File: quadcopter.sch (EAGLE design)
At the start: 75 parts, among them J1 AVR_SPI_PRG_6NS, J3 HEADER-0.1IN-2POS-FEMALE, J4 HEADER-0.1IN-2POS-FEMALE, J5 HEADER-0.1IN-2POS-FEMALE, J6 HEADER-0.1IN-2POS-FEMALE, SW1 PUSHBUTTON_SMD-VERTICAL, SW2 PUSHBUTTON_SMD-VERTICAL, U1 ATMEGA128RFA1

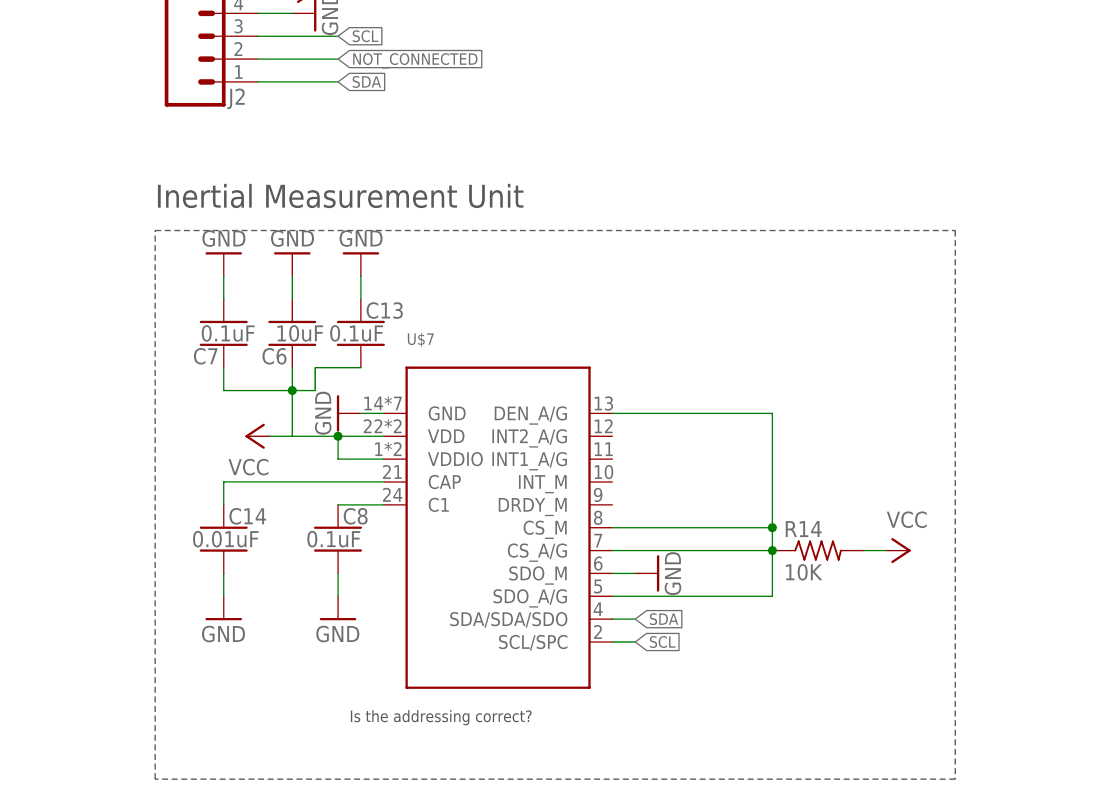
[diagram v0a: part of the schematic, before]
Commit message: added i2c pullups, placed oscillator components
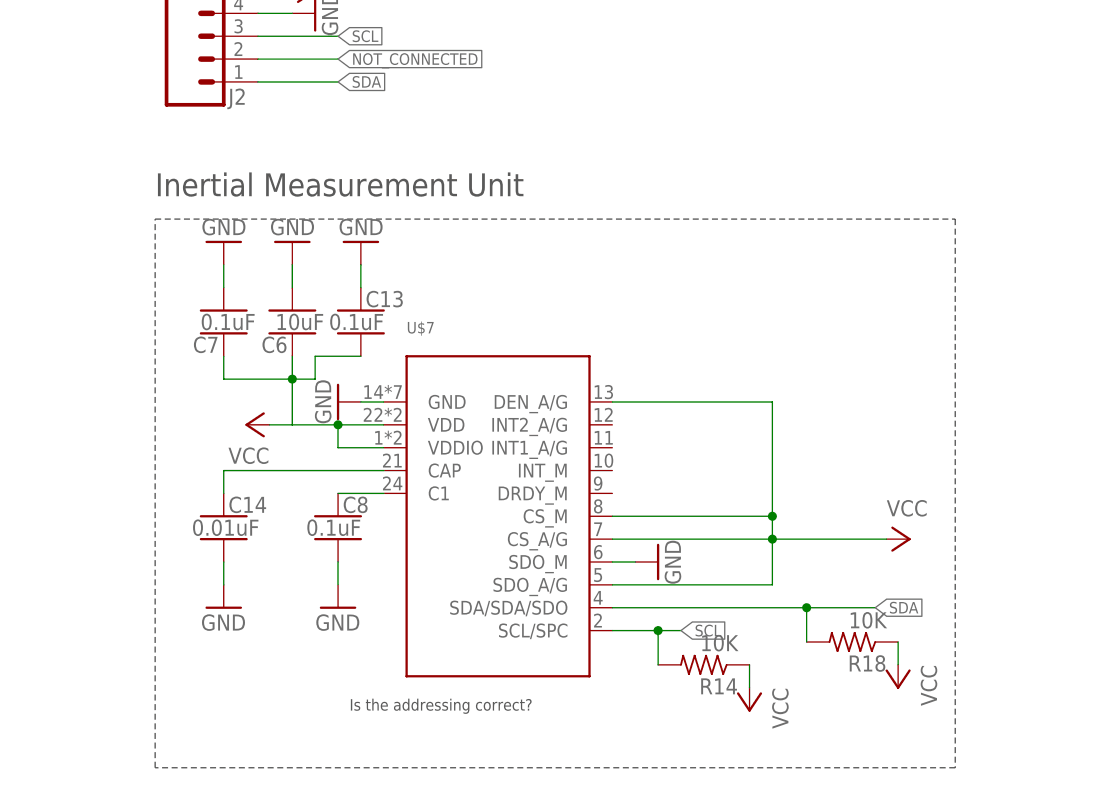
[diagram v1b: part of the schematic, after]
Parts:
- added R18: 10K, quadparts_prebuilt:RESISTOR_SMD-2012-0805-10K
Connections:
- removed net N$10: R14.1, U$7.CS_A/G, U$7.CS_M, U$7.DEN_A/G, U$7.SDO_A/G
- net SCL: now also R14.2
- net SDA: now also R18.2
- net VCC: now also R14.1, R18.1, U$7.CS_A/G, U$7.CS_M, U$7.DEN_A/G, U$7.SDO_A/G; no longer R14.2
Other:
- moved on the sheet: C13, C14, C6, C7, C8, R14, U$7

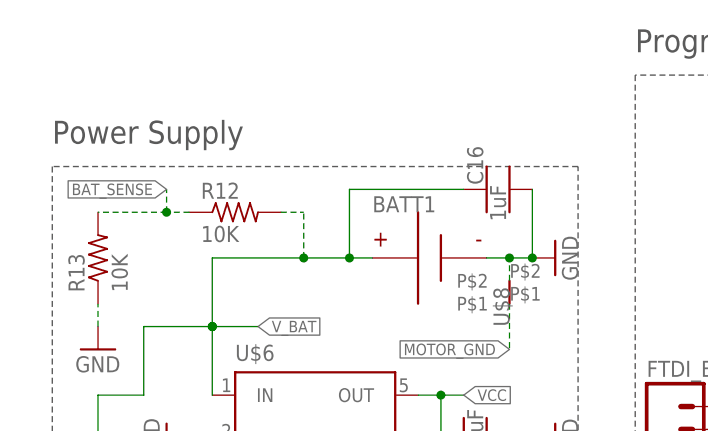
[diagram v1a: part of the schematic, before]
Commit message: layed down bat plane
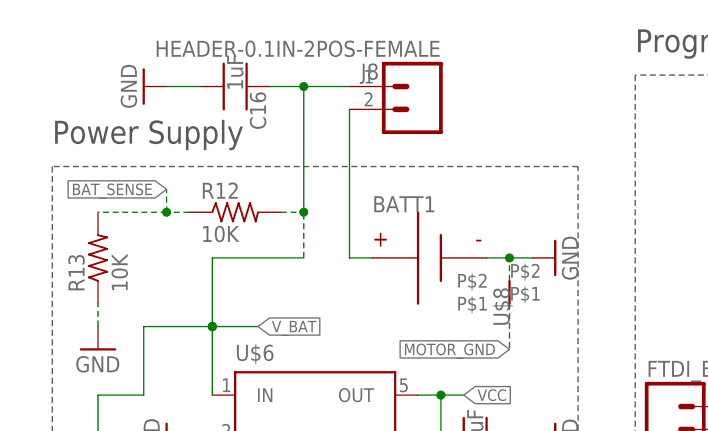
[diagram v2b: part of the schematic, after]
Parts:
- added J8: HEADER-0.1IN-2POS-FEMALE, Components:HEADER-0.1IN-2POS-FEMALE
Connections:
- new net N$10: BATT1.P, J8.2
- net V_BAT: now also J8.1; no longer BATT1.P
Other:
- moved on the sheet: C16
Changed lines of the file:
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@@
 <part name="P+12" library="quadparts_prebuilt" deviceset="VCC" device=""/>
 <part name="P+13" library="quadparts_prebuilt" deviceset="VCC" device=""/>
+<part name="J8" library="Components" deviceset="HEADER-0.1IN-2POS" device="-FEMALE"/>
+<part name="GND36" library="quadparts_prebuilt" deviceset="GND" device=""/>
 </parts>
 <sheets>
@@
 <instance part="GND30" gate="1" x="355.6" y="-195.58"/>
 <instance part="P+10" gate="VCC" x="256.54" y="-102.87"/>
-<instance part="C16" gate="G$1" x="60.96" y="-26.67" rot="R90"/>
+<instance part="C16" gate="G$1" x="34.29" y="-15.24" rot="R270"/>
 <instance part="C17" gate="G$1" x="60.96" y="-54.61" rot="R270"/>
 <instance part="GND11" gate="1" x="68.58" y="-54.61" rot="R90"/>
@@
 <instance part="P+12" gate="VCC" x="90.17" y="-234.95" rot="R180"/>
 <instance part="P+13" gate="VCC" x="106.68" y="-232.41" rot="R180"/>
+<instance part="J8" gate="G$1" x="55.88" y="-12.7" rot="R180"/>
+<instance part="GND36" gate="1" x="22.86" y="-15.24" rot="R270"/>
 </instances>
 <busses>
@@
 <wire x1="63.5" y1="-36.83" x2="63.5" y2="-34.29" width="0.1524" layer="91" style="longdash"/>
 <junction x="63.5" y="-34.29"/>
-<pinref part="C16" gate="G$1" pin="2"/>
-<wire x1="66.04" y1="-26.67" x2="66.04" y2="-34.29" width="0.1524" layer="91"/>
-<junction x="66.04" y="-34.29"/>
 </segment>
 <segment>
@@
 <wire x1="35.56" y1="-157.48" x2="39.37" y2="-157.48" width="0.1524" layer="91"/>
 <pinref part="GND25" gate="1" pin="GND"/>
+</segment>
+<segment>
+<pinref part="C16" gate="G$1" pin="2"/>
+<pinref part="GND36" gate="1" pin="GND"/>
+<wire x1="29.21" y1="-15.24" x2="25.4" y2="-15.24" width="0.1524" layer="91"/>
 </segment>
 </net>
@@
 <pinref part="R12" gate="G$1" pin="2"/>
 <wire x1="38.1" y1="-29.21" x2="40.64" y2="-29.21" width="0.1524" layer="91" style="longdash"/>
-<pinref part="BATT1" gate="G$1" pin="P"/>
-<wire x1="48.26" y1="-34.29" x2="45.72" y2="-34.29" width="0.1524" layer="91"/>
-<junction x="40.64" y="-34.29"/>
-<wire x1="45.72" y1="-34.29" x2="40.64" y2="-34.29" width="0.1524" layer="91"/>
 <wire x1="40.64" y1="-34.29" x2="40.64" y2="-29.21" width="0.1524" layer="91" style="longdash"/>
 <wire x1="40.64" y1="-34.29" x2="30.48" y2="-34.29" width="0.1524" layer="91"/>
 <wire x1="30.48" y1="-34.29" x2="30.48" y2="-41.91" width="0.1524" layer="91"/>
-<wire x1="45.72" y1="-34.29" x2="45.72" y2="-26.67" width="0.1524" layer="91"/>
-<junction x="45.72" y="-34.29"/>
-<wire x1="45.72" y1="-26.67" x2="58.42" y2="-26.67" width="0.1524" layer="91"/>
+<pinref part="J8" gate="G$1" pin="1"/>
+<wire x1="45.72" y1="-15.24" x2="40.64" y2="-15.24" width="0.1524" layer="91"/>
+<wire x1="40.64" y1="-15.24" x2="40.64" y2="-29.21" width="0.1524" layer="91"/>
+<junction x="40.64" y="-29.21"/>
 <pinref part="C16" gate="G$1" pin="1"/>
+<wire x1="40.64" y1="-15.24" x2="36.83" y2="-15.24" width="0.1524" layer="91"/>
+<junction x="40.64" y="-15.24"/>
 </segment>
 <segment>
@@
 </segment>
 </net>
+<net name="N$10" class="1">
+<segment>
+<pinref part="BATT1" gate="G$1" pin="P"/>
+<wire x1="48.26" y1="-34.29" x2="45.72" y2="-34.29" width="0.1524" layer="91"/>
+<pinref part="J8" gate="G$1" pin="2"/>
+<wire x1="45.72" y1="-34.29" x2="45.72" y2="-17.78" width="0.1524" layer="91"/>
+</segment>
+</net>

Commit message: Layed out power planes
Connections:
- net MOTOR_GND renamed BAT_GND
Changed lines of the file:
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@@
 </segment>
 </net>
-<net name="MOTOR_GND" class="1">
+<net name="BAT_GND" class="1">
 <segment>
 <pinref part="C21" gate="G$1" pin="2"/>

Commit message: further isolated attenna
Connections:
- net BAT_GND: now also C9.-
- net GND: no longer C9.-
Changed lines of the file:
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@@
 <setting verticaltext="up"/>
 </settings>
-<grid distance="0.05" unitdist="inch" unit="inch" style="lines" multiple="1" display="no" altdistance="0.01" altunitdist="inch" altunit="inch"/>
+<grid distance="0.1" unitdist="inch" unit="inch" style="lines" multiple="1" display="no" altdistance="0.01" altunitdist="inch" altunit="inch"/>
 <layers>
 <layer number="1" name="Top" color="4" fill="1" visible="no" active="no"/>
@@
 <part name="R17" library="quadparts_prebuilt" deviceset="RESISTOR_" device="SMD-2012-0805-330" value="330"/>
 <part name="GND29" library="quadparts_prebuilt" deviceset="GND" device=""/>
-<part name="GND30" library="quadparts_prebuilt" deviceset="GND" device=""/>
 <part name="P+10" library="quadparts_prebuilt" deviceset="VCC" device=""/>
 <part name="C16" library="quadparts_prebuilt" deviceset="CAPACITOR-NP_" device="SMD-2012-0805_CERAMIC-1UF" value="1uF"/>
@@
 <instance part="R17" gate="G$1" x="167.64" y="-175.26"/>
 <instance part="GND29" gate="1" x="142.24" y="-175.26" rot="R270"/>
-<instance part="GND30" gate="1" x="355.6" y="-195.58"/>
 <instance part="P+10" gate="VCC" x="256.54" y="-102.87"/>
 <instance part="C16" gate="G$1" x="34.29" y="-15.24" rot="R270"/>
@@
 </segment>
 <segment>
-<pinref part="C9" gate="G$1" pin="-"/>
-<wire x1="355.6" y1="-190.5" x2="355.6" y2="-193.04" width="0.1524" layer="91"/>
-<pinref part="GND30" gate="1" pin="GND"/>
-</segment>
-<segment>
 <pinref part="C17" gate="G$1" pin="1"/>
 <pinref part="GND11" gate="1" pin="GND"/>
@@
 <label x="63.5" y="-44.45" size="1.27" layer="95" font="fixed" rot="R180" xref="yes"/>
 </segment>
-</net>
+<segment>
+<pinref part="C9" gate="G$1" pin="-"/>
+<wire x1="355.6" y1="-190.5" x2="355.6" y2="-193.04" width="0.1524" layer="91"/>
+<label x="355.6" y="-193.04" size="1.27" layer="95" font="fixed" rot="R180" xref="yes"/>
+</segment>
+</net>

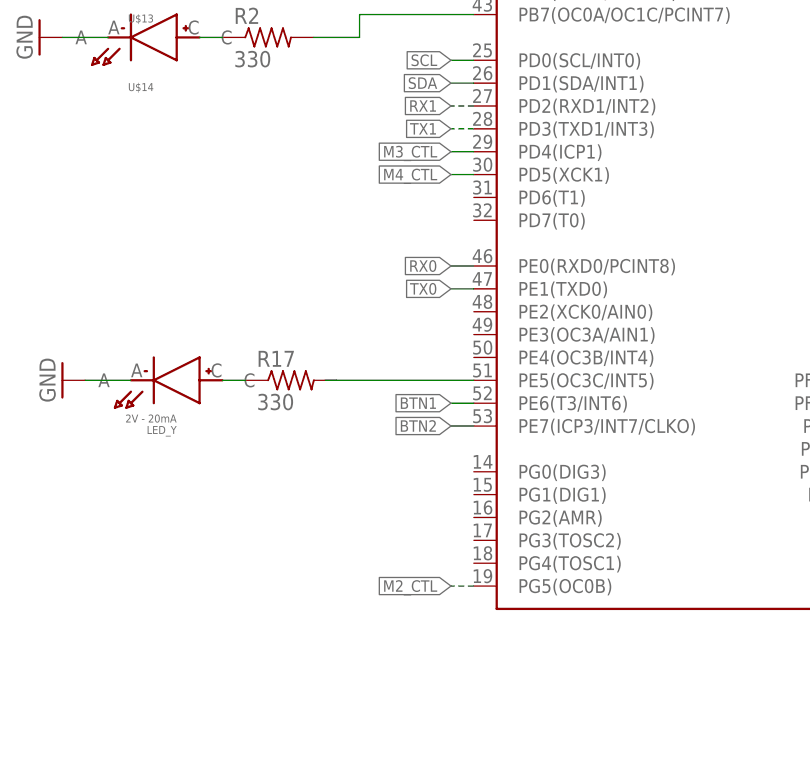
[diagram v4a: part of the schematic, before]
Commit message: swaped motor 2 and 4
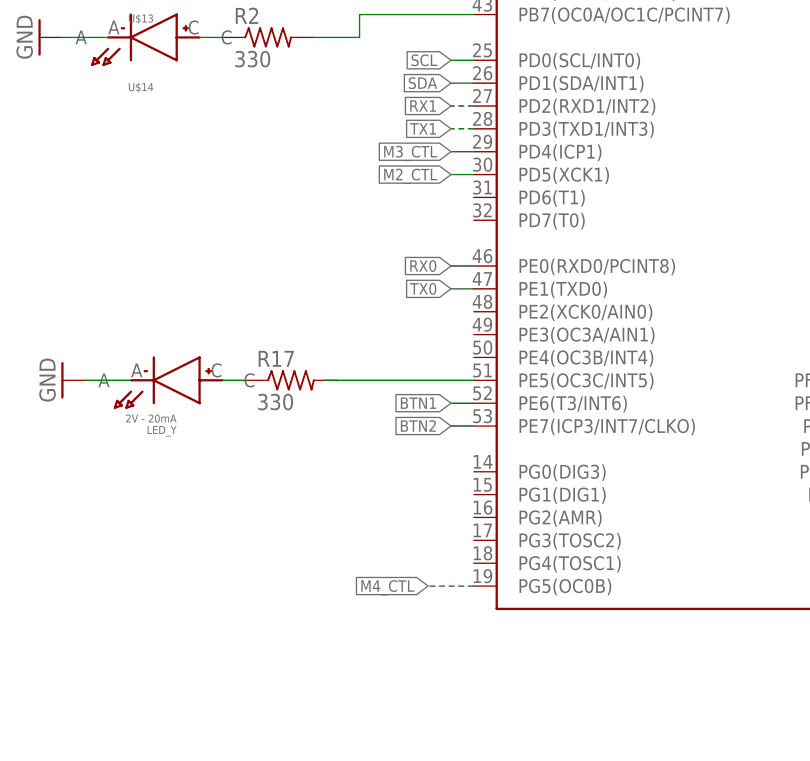
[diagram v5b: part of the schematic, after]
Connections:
- net M2_CTL: now also U1.PD5(XCK1); no longer U1.PG5(OC0B)
- net M4_CTL: now also U1.PG5(OC0B); no longer U1.PD5(XCK1)
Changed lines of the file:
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@@
 </segment>
 <segment>
-<pinref part="U1" gate="G$1" pin="PD5(XCK1)"/>
-<wire x1="187.96" y1="-152.4" x2="185.42" y2="-152.4" width="0.1524" layer="91"/>
-<label x="185.42" y="-152.4" size="1.27" layer="95" font="fixed" rot="MR0" xref="yes"/>
+<pinref part="U1" gate="G$1" pin="PG5(OC0B)"/>
+<wire x1="187.96" y1="-198.12" x2="182.88" y2="-198.12" width="0.1524" layer="91" style="longdash"/>
+<label x="182.88" y="-198.12" size="1.27" layer="95" font="fixed" rot="R180" xref="yes"/>
 </segment>
 </net>
@@
 </segment>
 <segment>
-<pinref part="U1" gate="G$1" pin="PG5(OC0B)"/>
-<wire x1="187.96" y1="-198.12" x2="185.42" y2="-198.12" width="0.1524" layer="91" style="longdash"/>
-<label x="185.42" y="-198.12" size="1.27" layer="95" font="fixed" rot="R180" xref="yes"/>
+<pinref part="U1" gate="G$1" pin="PD5(XCK1)"/>
+<wire x1="187.96" y1="-152.4" x2="185.42" y2="-152.4" width="0.1524" layer="91"/>
+<label x="185.42" y="-152.4" size="1.27" layer="95" font="fixed" rot="MR0" xref="yes"/>
 </segment>
 </net>

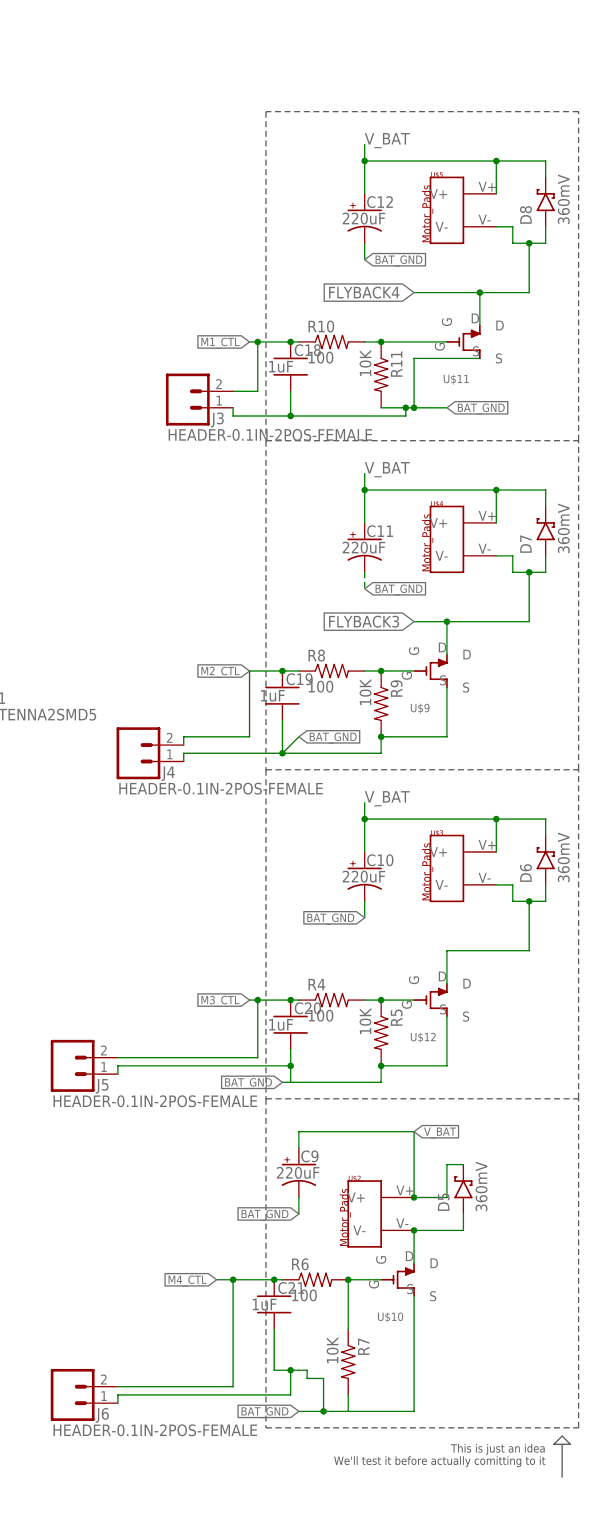
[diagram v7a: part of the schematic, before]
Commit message: fixed pwm filters
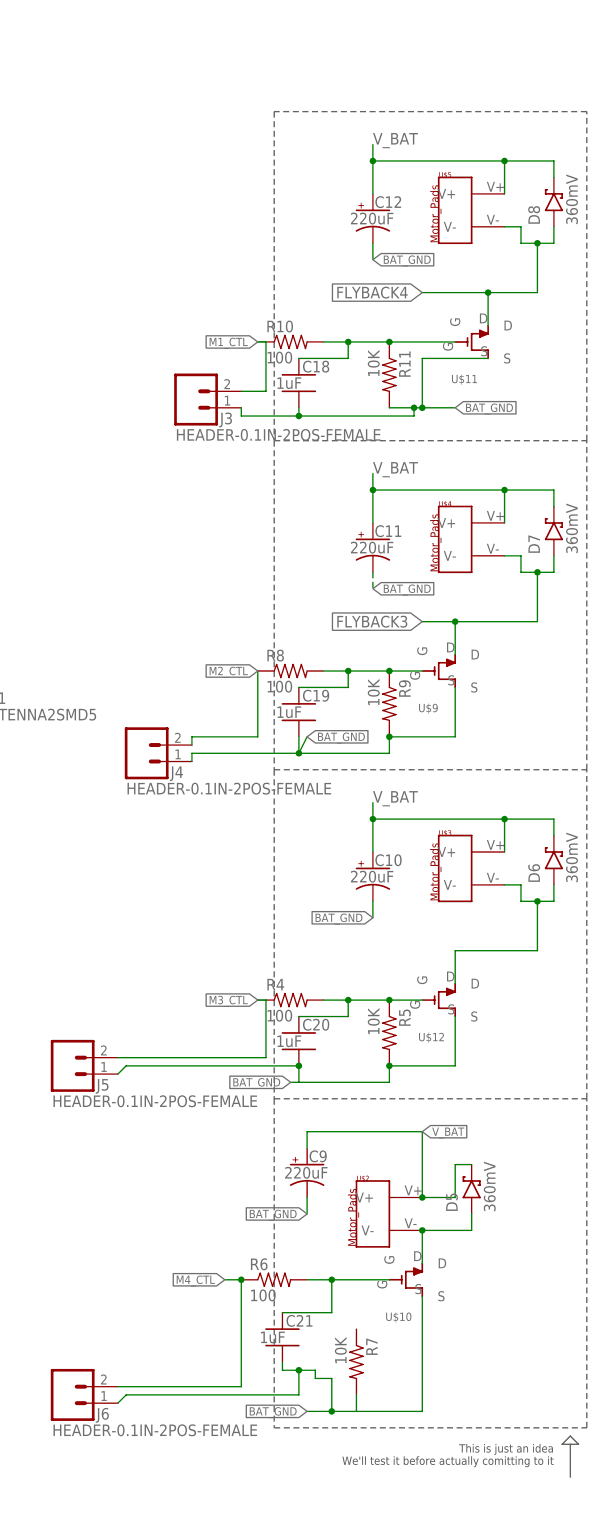
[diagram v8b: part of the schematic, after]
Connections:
- net M1_CTL: no longer C18.1
- net M2_CTL: no longer C19.1
- net M3_CTL: no longer C20.1
- net M4_CTL: no longer C21.1
- net N$11: now also C19.1
- net N$12: now also C21.1; no longer R7.1
- net N$13: now also C18.1
- net N$8: now also C20.1
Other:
- moved on the sheet: C10, C11, C12, C18, C19, C20, C21, C9, D5, D6, D7, D8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
